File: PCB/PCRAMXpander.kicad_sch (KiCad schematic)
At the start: 22 parts, among them J1 Bus_ISA_16bit, U1 ATF16V8B-15PU, U2 SN74LVC16245ADGGR, U3 SN74LVC16244ADGGR, U4 SN74LVC16244ADGGR, U5 AS6C3216A-55TIN, U6 AS6C3216A-55TIN

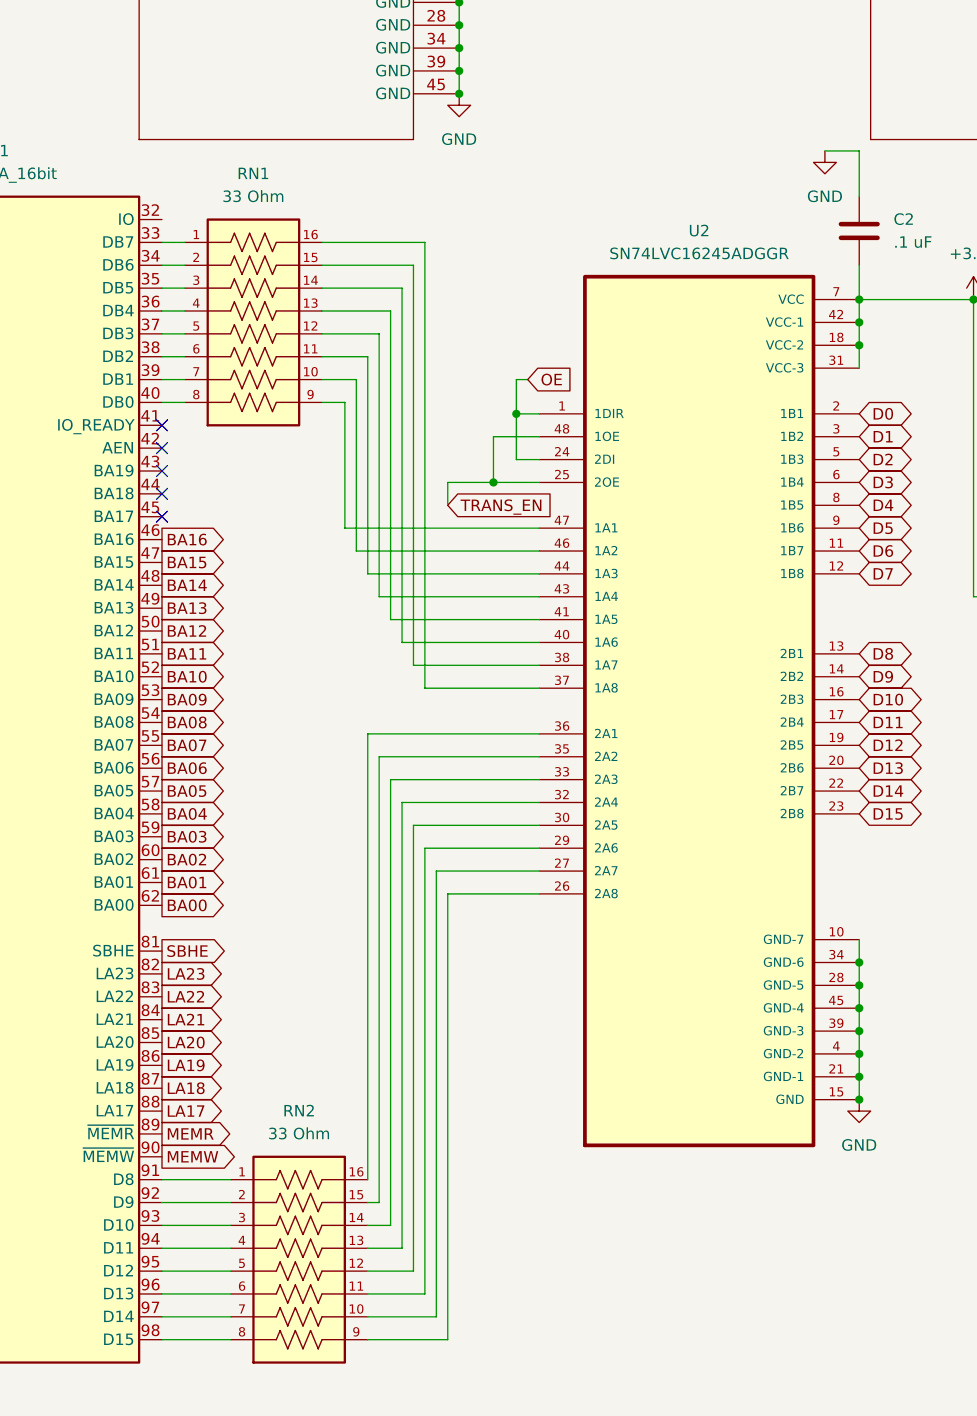
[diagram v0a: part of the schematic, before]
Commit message: Switching to 245 w/ built-in resistors
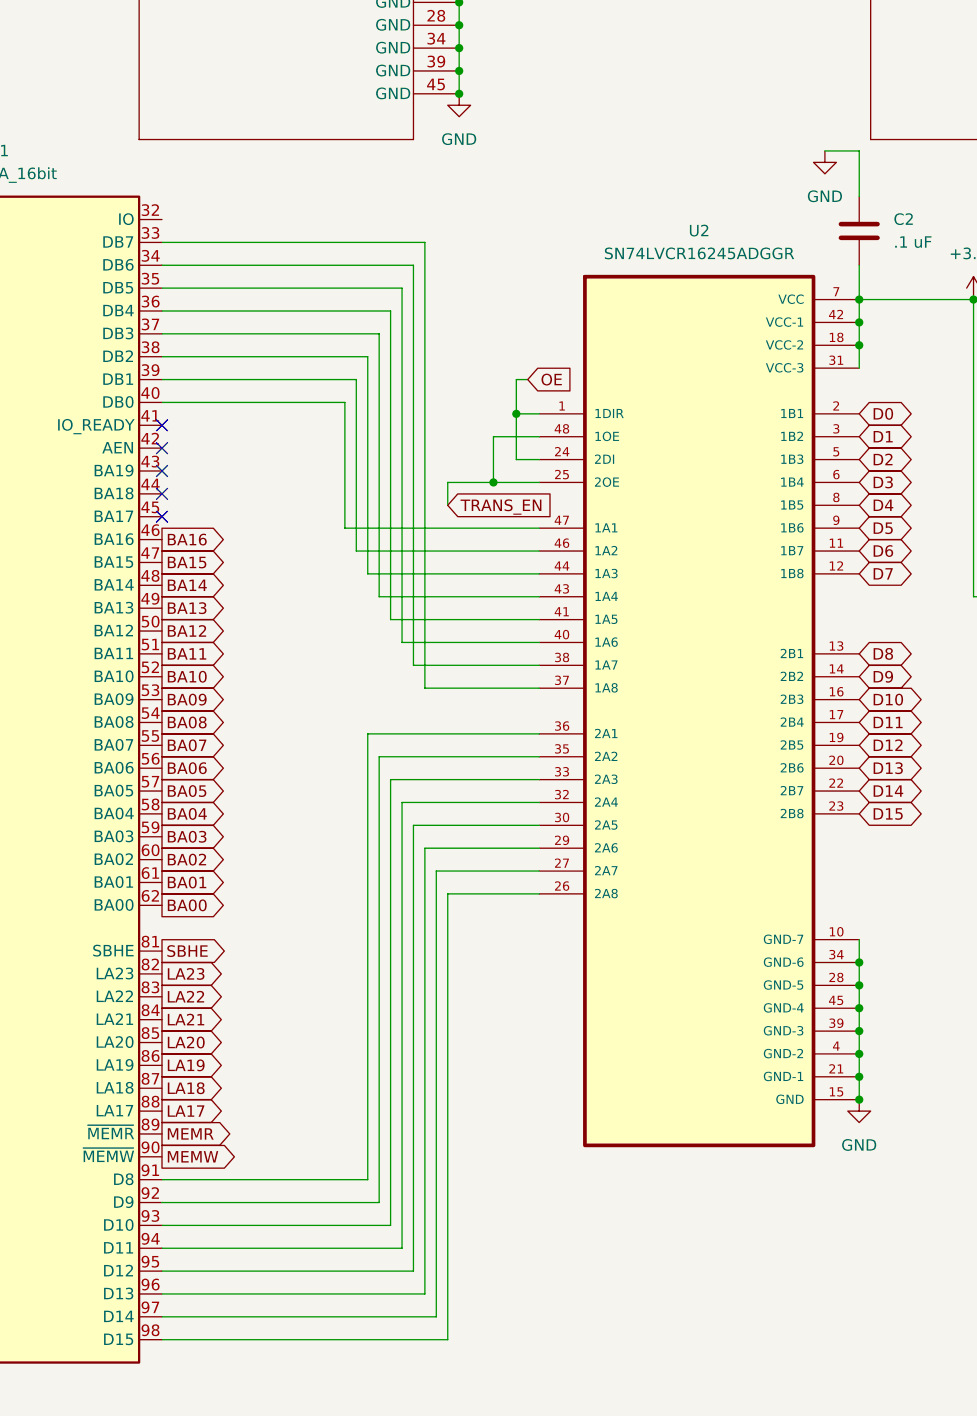
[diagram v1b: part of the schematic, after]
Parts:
- removed RN1, RN2: 33 Ohm, Project:RESCAXE50P380X160X55-16N, symbol EXB-2HV330JV:EXB-2HV330JV
- removed U2: SN74LVC16245ADGGR, Project:SOP50P810X120-48N, symbol SN74LVC16245ADGGR:SN74LVC16245ADGGR
- added U2: SN74LVCR16245ADGGR, Project:SOP50P810X120-48N, symbol SN74LVCR16245ADGGR:SN74LVCR16245ADGGR
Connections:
- net +3.3V: now also U2.18 (VCC-2), U2.31 (VCC-3), U2.42 (VCC-1), U2.7 (VCC)
- net D0: now also U2.2 (1B1)
- net D1: now also U2.3 (1B2)
- net D10: now also U2.16 (2B3)
- net D11: now also U2.17 (2B4)
- net D12: now also U2.19 (2B5)
- net D13: now also U2.20 (2B6)
- net D14: now also U2.22 (2B7)
- net D15: now also U2.23 (2B8)
- net D2: now also U2.5 (1B3)
- net D3: now also U2.6 (1B4)
- net D4: now also U2.8 (1B5)
- net D5: now also U2.9 (1B6)
- net D6: now also U2.11 (1B7)
- net D7: now also U2.12 (1B8)
- net D8: now also U2.13 (2B1)
- net D9: now also U2.14 (2B2)
- net GND: now also U2.10 (GND-7), U2.15 (GND), U2.21 (GND-1), U2.28 (GND-5), U2.34 (GND-6), U2.39 (GND-3), U2.4 (GND-2), U2.45 (GND-4)
- net OE: now also U2.1 (1DIR), U2.24 (2DI)
- net TRANS_EN: now also U2.25 (2OE), U2.48 (1OE)
- net at J1.33 (DB7): now also U2.37 (1A8)
- net at J1.34 (DB6): now also U2.38 (1A7)
- net at J1.35 (DB5): now also U2.40 (1A6)
- net at J1.36 (DB4): now also U2.41 (1A5)
- net at J1.37 (DB3): now also U2.43 (1A4)
- net at J1.38 (DB2): now also U2.44 (1A3)
- net at J1.39 (DB1): now also U2.46 (1A2)
- net at J1.40 (DB0): now also U2.47 (1A1)
- net at J1.91 (D8): now also U2.36 (2A1)
- net at J1.92 (D9): now also U2.35 (2A2)
- net at J1.93 (D10): now also U2.33 (2A3)
- net at J1.94 (D11): now also U2.32 (2A4)
- net at J1.95 (D12): now also U2.30 (2A5)
- net at J1.96 (D13): now also U2.29 (2A6)
- net at J1.97 (D14): now also U2.27 (2A7)
- net at J1.98 (D15): now also U2.26 (2A8)

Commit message: Routing has begun
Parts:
- added R2, R3, R4: 10k, symbol Device:R
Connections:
- net +3.3V: now also R4.1
- net +5V: now also R2.1, R3.2
- net WE: now also R4.2
- net at JP1.2 (B), U1.5 (I4): now also R2.2; no longer R1.2
- net at JP2.2 (B), U1.6 (I5): now also R3.1; no longer R1.10
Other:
- moved on the sheet: JP1

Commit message: Playing with routing a bit more
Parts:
- removed R4: 10k, symbol Device:R
- R1: renamed from R2; footprint (none) -> Resistor_SMD:R_0805_2012Metric_Pad1.20x1.40mm_HandSolder
- R2: renamed from R3; footprint (none) -> Resistor_SMD:R_0805_2012Metric_Pad1.20x1.40mm_HandSolder
- renumbered R1 to R3
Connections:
- net C1E: now also R3.10; no longer R3.3
- net C2E: now also R3.7; no longer R3.4
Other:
- moved on the sheet: R3

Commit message: More manual routing
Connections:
- net C2E: now also R3.9; no longer R3.7
- net WE: now also R3.7; no longer R3.9
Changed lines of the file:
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@@
 	(global_label "WE"
 		(shape output)
-		(at 350.52 69.85 0)
-		(fields_autoplaced yes)
-		(effects
-			(font
-				(size 1.27 1.27)
-			)
-			(justify left)
-		)
-		(property "Intersheetrefs" "${INTERSHEET_REFS}"
-			(at 356.1056 69.85 0)
+		(at 350.52 85.09 0)
+		(fields_autoplaced yes)
+		(effects
+			(font
+				(size 1.27 1.27)
+			)
+			(justify left)
+		)
+		(property "Intersheetrefs" "${INTERSHEET_REFS}"
+			(at 356.1056 85.09 0)
 			(effects
 				(font
@@
 	(global_label "C2E"
 		(shape input)
-		(at 350.52 85.09 0)
-		(fields_autoplaced yes)
-		(effects
-			(font
-				(size 1.27 1.27)
-			)
-			(justify left)
-		)
-		(property "Intersheetrefs" "${INTERSHEET_REFS}"
-			(at 357.1337 85.09 0)
-			(effects
-				(font
+		(at 350.52 69.85 0)
+		(fields_autoplaced yes)
+		(effects
+			(font
+				(size 1.27 1.27)
+			)
+			(justify left)
+		)
+		(property "Intersheetrefs" "${INTERSHEET_REFS}"
+			(at 357.1337 69.85 0)
+			(effects
+				(font

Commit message: Revert "More manual routing"
This reverts commit 47449c23b7240c85fd4465f78316c60ac3030f38.
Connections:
- net C2E: now also R3.7; no longer R3.9
- net WE: now also R3.9; no longer R3.7
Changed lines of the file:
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@@
 	(global_label "WE"
 		(shape output)
-		(at 350.52 85.09 0)
-		(fields_autoplaced yes)
-		(effects
-			(font
-				(size 1.27 1.27)
-			)
-			(justify left)
-		)
-		(property "Intersheetrefs" "${INTERSHEET_REFS}"
-			(at 356.1056 85.09 0)
+		(at 350.52 69.85 0)
+		(fields_autoplaced yes)
+		(effects
+			(font
+				(size 1.27 1.27)
+			)
+			(justify left)
+		)
+		(property "Intersheetrefs" "${INTERSHEET_REFS}"
+			(at 356.1056 69.85 0)
 			(effects
 				(font
@@
 	(global_label "C2E"
 		(shape input)
-		(at 350.52 69.85 0)
-		(fields_autoplaced yes)
-		(effects
-			(font
-				(size 1.27 1.27)
-			)
-			(justify left)
-		)
-		(property "Intersheetrefs" "${INTERSHEET_REFS}"
-			(at 357.1337 69.85 0)
-			(effects
-				(font
+		(at 350.52 85.09 0)
+		(fields_autoplaced yes)
+		(effects
+			(font
+				(size 1.27 1.27)
+			)
+			(justify left)
+		)
+		(property "Intersheetrefs" "${INTERSHEET_REFS}"
+			(at 357.1337 85.09 0)
+			(effects
+				(font

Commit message: SIP5 resistor pack
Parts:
- removed R3: 10 kOhm, Project:RESCAV80P400X210X65-10N, symbol EXB-E10C103J:EXB-E10C103J
- added R3: 10k, Project:CSC05_VIS, symbol CSC05A0110K0GEK_2026-01-04_16-49-05:CSC05A0110K0GEK
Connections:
- net +3.3V: now also R3.1
- net C1E: now also R3.5
- net C2E: now also R3.2
- net WE: now also R3.4
- no-connect marks 55 -> 53
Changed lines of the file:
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@@
 	)
 	(no_connect
-		(at 314.96 85.09)
-	)
-	(no_connect
 		(at 134.62 190.5)
 	)
@@
 	)
 	(no_connect
-		(at 314.96 62.23)
-	)
-	(no_connect
 		(at 134.62 167.64)
 	)
@@
 	(wire
 		(pts
+			(xy 328.93 107.95) (xy 328.93 111.76)
+		)
+		(stroke
+			(width 0)
+			(type default)
+		)
+	)
+	(wire
+		(pts
 			(xy 313.69 173.99) (xy 323.85 173.99)
 		)
@@
 	(wire
 		(pts
-			(xy 312.42 54.61) (xy 314.96 54.61)
-		)
-		(stroke
-			(width 0)
-			(type default)
-		)
-	)
-	(wire
-		(pts
 			(xy 203.2 107.95) (xy 203.2 110.49)
 		)
@@
 	(global_label "OE"
 		(shape output)
-		(at 350.52 77.47 0)
+		(at 334.01 113.03 90)
 		(fields_autoplaced yes)
 		(effects
@@
 		)
 		(property "Intersheetrefs" "${INTERSHEET_REFS}"
-			(at 355.9847 77.47 0)
+			(at 334.01 107.5653 90)
 			(effects
 				(font
@@
 	(global_label "C1E"
 		(shape input)
-		(at 350.52 62.23 0)
+		(at 339.09 107.95 270)
 		(fields_autoplaced yes)
 		(effects
@@
 				(size 1.27 1.27)
 			)
-			(justify left)
+			(justify right)
 		)
 		(property "Intersheetrefs" "${INTERSHEET_REFS}"
-			(at 357.1337 62.23 0)
+			(at 339.09 114.5637 90)
 			(effects
 				(font
 					(size 1.27 1.27)
 				)
-				(justify left)
+				(justify right)
 				(hide yes)
 			)
@@
 	)
 	(global_label "WE"
-		(shape output)
-		(at 350.52 69.85 0)
+		(shape input)
+		(at 336.55 107.95 270)
 		(fields_autoplaced yes)
 		(effects
@@
 				(size 1.27 1.27)
 			)
-			(justify left)
+			(justify right)
 		)
 		(property "Intersheetrefs" "${INTERSHEET_REFS}"
-			(at 356.1056 69.85 0)
+			(at 336.55 113.5356 90)
 			(effects
 				(font
 					(size 1.27 1.27)
 				)
-				(justify left)
+				(justify right)
 				(hide yes)
 			)
@@
 	(global_label "C2E"
 		(shape input)
-		(at 350.52 85.09 0)
+		(at 331.47 107.95 270)
 		(fields_autoplaced yes)
 		(effects
@@
 				(size 1.27 1.27)
 			)
-			(justify left)
+			(justify right)
 		)
 		(property "Intersheetrefs" "${INTERSHEET_REFS}"
-			(at 357.1337 85.09 0)
+			(at 331.47 114.5637 90)
 			(effects
 				(font
 					(size 1.27 1.27)
 				)
-				(justify left)
+				(justify right)
 				(hide yes)
 			)
@@
 	(symbol
 		(lib_id "power:+3.3V")
-		(at 312.42 54.61 0)
+		(at 328.93 111.76 180)
 		(unit 1)
 		(exclude_from_sim no)
@@
 		(dnp no)
 		(property "Reference" "#PWR05"
-			(at 312.42 58.42 0)
+			(at 328.93 107.95 0)
 			(effects
 				(font
@@
 		)
 		(property "Value" "+3.3V"
-			(at 312.42 49.53 0)
+			(at 328.93 116.84 0)
 			(effects
 				(font
@@
 		)
 		(property "Footprint" ""
-			(at 312.42 54.61 0)
+			(at 328.93 111.76 0)
 			(effects
 				(font
@@
 		)
 		(property "Datasheet" ""
-			(at 312.42 54.61 0)
+			(at 328.93 111.76 0)
 			(effects
 				(font
@@
 		)
 		(property "Description" "Power symbol creates a global label with name \"+3.3V\""
-			(at 312.42 54.61 0)
+			(at 328.93 111.76 0)
 			(effects
 				(font
@@
 	)
 	(symbol
-		(lib_id "EXB-E10C103J:EXB-E10C103J")
-		(at 332.74 69.85 0)
-		(unit 1)
-		(exclude_from_sim no)
-		(in_bom yes)
-		(on_board yes)
-		(dnp no)
-		(fields_autoplaced yes)
-		(property "Reference" "R3"
-			(at 332.74 44.45 0)
-			(effects
-				(font
-					(size 1.27 1.27)
-				)
-			)
-		)
-		(property "Value" "10 kOhm"
-			(at 332.74 46.99 0)
-			(effects
-				(font
-					(size 1.27 1.27)
-				)
-			)
-		)
-		(property "Footprint" "Project:RESCAV80P400X210X65-10N"
-			(at 332.74 69.85 0)
-			(effects
-				(font
-					(size 1.27 1.27)
-				)
-				(justify bottom)
-				(hide yes)
-			)
-		)
-		(property "Datasheet" ""
-			(at 332.74 69.85 0)
-			(effects
-				(font
-					(size 1.27 1.27)
-				)
-				(hide yes)
-			)
-		)
-		(property "Description" ""
-			(at 332.74 69.85 0)
-			(effects
-				(font
-					(size 1.27 1.27)
-				)
-				(hide yes)
-			)
-		)
-		(property "PARTREV" "1-Mar-20"
-			(at 332.74 69.85 0)
-			(effects
-				(font
-					(size 1.27 1.27)
-				)
-				(justify bottom)
-				(hide yes)
-			)
-		)
-		(property "STANDARD" "IPC 7351B"
-			(at 332.74 69.85 0)
-			(effects
-				(font
-					(size 1.27 1.27)
-				)
-				(justify bottom)
-				(hide yes)
-			)
-		)
-		(property "MAXIMUM_PACKAGE_HEIGHT" "0.65 mm"
-			(at 332.74 69.85 0)
-			(effects
-				(font
-					(size 1.27 1.27)
-				)
-				(justify bottom)
-				(hide yes)
-			)
-		)
-		(property "MANUFACTURER" "Panasonic"
-			(at 332.74 69.85 0)
-			(effects
-				(font
-					(size 1.27 1.27)
-				)
-				(justify bottom)
-				(hide yes)
-			)
-		)
-		(pin "2"
-		)
-		(pin "6"
-		)
-		(pin "1"
-		)
-		(pin "9"
-		)
-		(pin "8"
-		)
-		(pin "7"
-		)
-		(pin "3"
-		)
-		(pin "4"
-		)
-		(pin "5"
-		)
-		(pin "10"
-		)
-		(instances
-			(project ""
-				(path "/1cf6e2a4-b983-419d-81f7-8fbd15ee10a7"
-					(reference "R3")
-					(unit 1)
-				)
-			)
-		)
-	)
-	(symbol
 		(lib_id "Jumper:Jumper_2_Open")
 		(at 26.67 185.42 0)
@@
 					(unit 1)
 				)
+			)
+		)
+	)
+	(symbol
+		(lib_id "CSC05A0110K0GEK_2026-01-04_16-49-05:CSC05A0110K0GEK")
+		(at 328.93 107.95 0)
+		(unit 1)
+		(exclude_from_sim no)
+		(in_bom yes)
+		(on_board yes)
+		(dnp no)
+		(fields_autoplaced yes)
+		(property "Reference" "R3"
+			(at 341.63 99.0789 0)
+			(effects
+				(font
+					(size 1.524 1.524)
+				)
+				(justify left)
+			)
+		)
+		(property "Value" "10k"
+			(at 341.63 101.6189 0)
+			(effects
+				(font
+					(size 1.524 1.524)
+				)
+				(justify left)
+			)
+		)
+		(property "Footprint" "Project:CSC05_VIS"
+			(at 328.93 107.95 0)
+			(effects
+				(font
+					(size 1.27 1.27)
+					(italic yes)
+				)
+				(hide yes)
+			)
+		)
+		(property "Datasheet" "https://www.vishay.com/doc?31509"
+			(at 328.93 107.95 0)
+			(effects
+				(font
+					(size 1.27 1.27)
+					(italic yes)
+				)
+				(hide yes)
+			)
+		)
+		(property "Description" ""
+			(at 328.93 107.95 0)
+			(effects
+				(font
+					(size 1.27 1.27)
+				)
+				(hide yes)
+			)
+		)
+		(pin "1"
+		)
+		(pin "2"
+		)
+		(pin "3"
+		)
+		(pin "4"
+		)
+		(pin "5"
+		)
+		(instances
+			(project ""
+				(path "/1cf6e2a4-b983-419d-81f7-8fbd15ee10a7"
+					(reference "R3")
+					(unit 1)
+				)

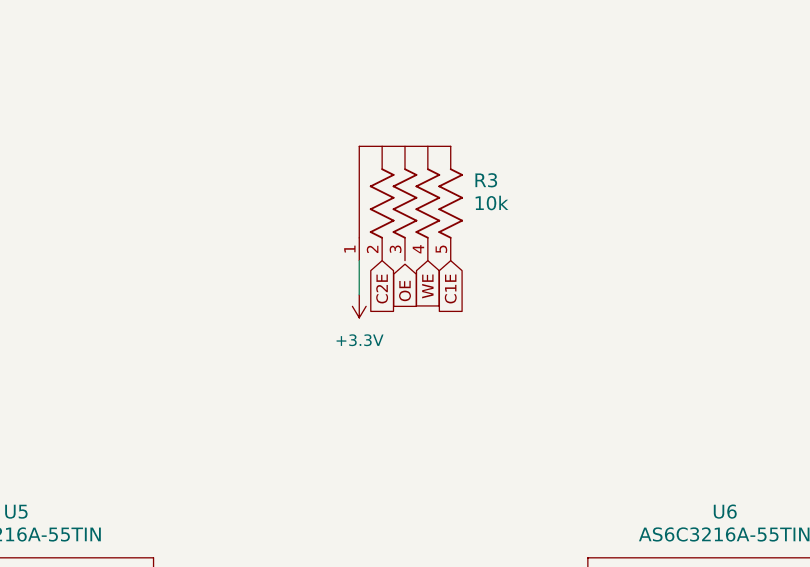
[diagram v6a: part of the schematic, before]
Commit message: U6 routing
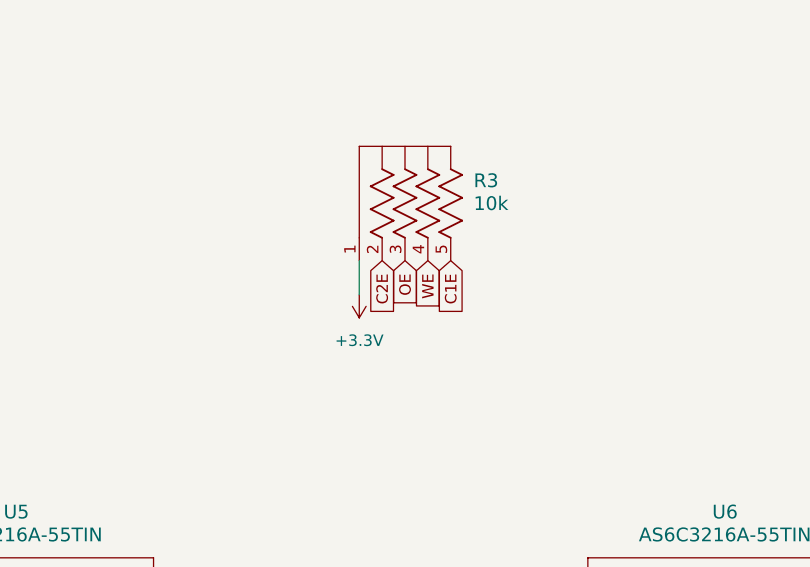
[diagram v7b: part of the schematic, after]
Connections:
- net OE: now also R3.3
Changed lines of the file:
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@@
 	)
 	(global_label "OE"
-		(shape output)
-		(at 334.01 113.03 90)
+		(shape input)
+		(at 334.01 107.95 270)
 		(fields_autoplaced yes)
 		(effects
@@
 				(size 1.27 1.27)
 			)
-			(justify left)
+			(justify right)
 		)
 		(property "Intersheetrefs" "${INTERSHEET_REFS}"
-			(at 334.01 107.5653 90)
+			(at 334.01 113.4147 90)
 			(effects
 				(font
 					(size 1.27 1.27)
 				)
-				(justify left)
+				(justify right)
 				(hide yes)
 			)
